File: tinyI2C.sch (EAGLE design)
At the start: 28 parts, among them IC1 74ABT125BQ, IC2 TPS76318, U1 LPC824M201JHI33, X1 TSW-112-02-S-S, X2 TSW-106-02-S-S-RA, X3 TSW-112-02-S-S, X4 TSW-102-02-S-S

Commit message: fiducials
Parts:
- added TP4, TP5: TPTP10R, testpad:TPTP10R
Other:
- note added: "FIDUCIALS"
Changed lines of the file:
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@@
 <part name="X4" library="con-samtec.local" deviceset="TSW-102-02-S-S" device=""/>
 <part name="GND12" library="mbed-HDK" deviceset="GND" device=""/>
+<part name="TP4" library="testpad" deviceset="TP" device="TP10R" value="TPTP10R"/>
+<part name="TP5" library="testpad" deviceset="TP" device="TP10R" value="TPTP10R"/>
 </parts>
 <sheets>
 <sheet>
 <plain>
+<text x="231.14" y="40.64" size="1.778" layer="91">FIDUCIALS</text>
 </plain>
 <instances>
@@
 <instance part="X4" gate="-2" x="83.82" y="122.428" rot="MR0"/>
 <instance part="GND12" gate="1" x="86.36" y="122.428"/>
+<instance part="TP4" gate="G$1" x="238.76" y="48.26" smashed="yes" rot="R90">
+<attribute name="NAME" x="238.252" y="47.244" size="1.778" layer="95" rot="MR0"/>
+<attribute name="TP_SIGNAL_NAME" x="240.03" y="49.53" size="1.778" layer="97" rot="R90"/>
+</instance>
+<instance part="TP5" gate="G$1" x="238.76" y="45.72" smashed="yes" rot="R90">
+<attribute name="NAME" x="238.252" y="44.704" size="1.778" layer="95" rot="MR0"/>
+<attribute name="TP_SIGNAL_NAME" x="240.03" y="46.99" size="1.778" layer="97" rot="R90"/>
+</instance>
 </instances>
 <busses>
@@
 </segment>
 </net>
+<net name="N$2" class="0">
+<segment>
+<wire x1="228.6" y1="53.34" x2="246.38" y2="53.34" width="0.1524" layer="91"/>
+<wire x1="246.38" y1="53.34" x2="246.38" y2="38.1" width="0.1524" layer="91"/>
+<wire x1="246.38" y1="38.1" x2="228.6" y2="38.1" width="0.1524" layer="91"/>
+<wire x1="228.6" y1="38.1" x2="228.6" y2="53.34" width="0.1524" layer="91"/>
+</segment>
+</net>

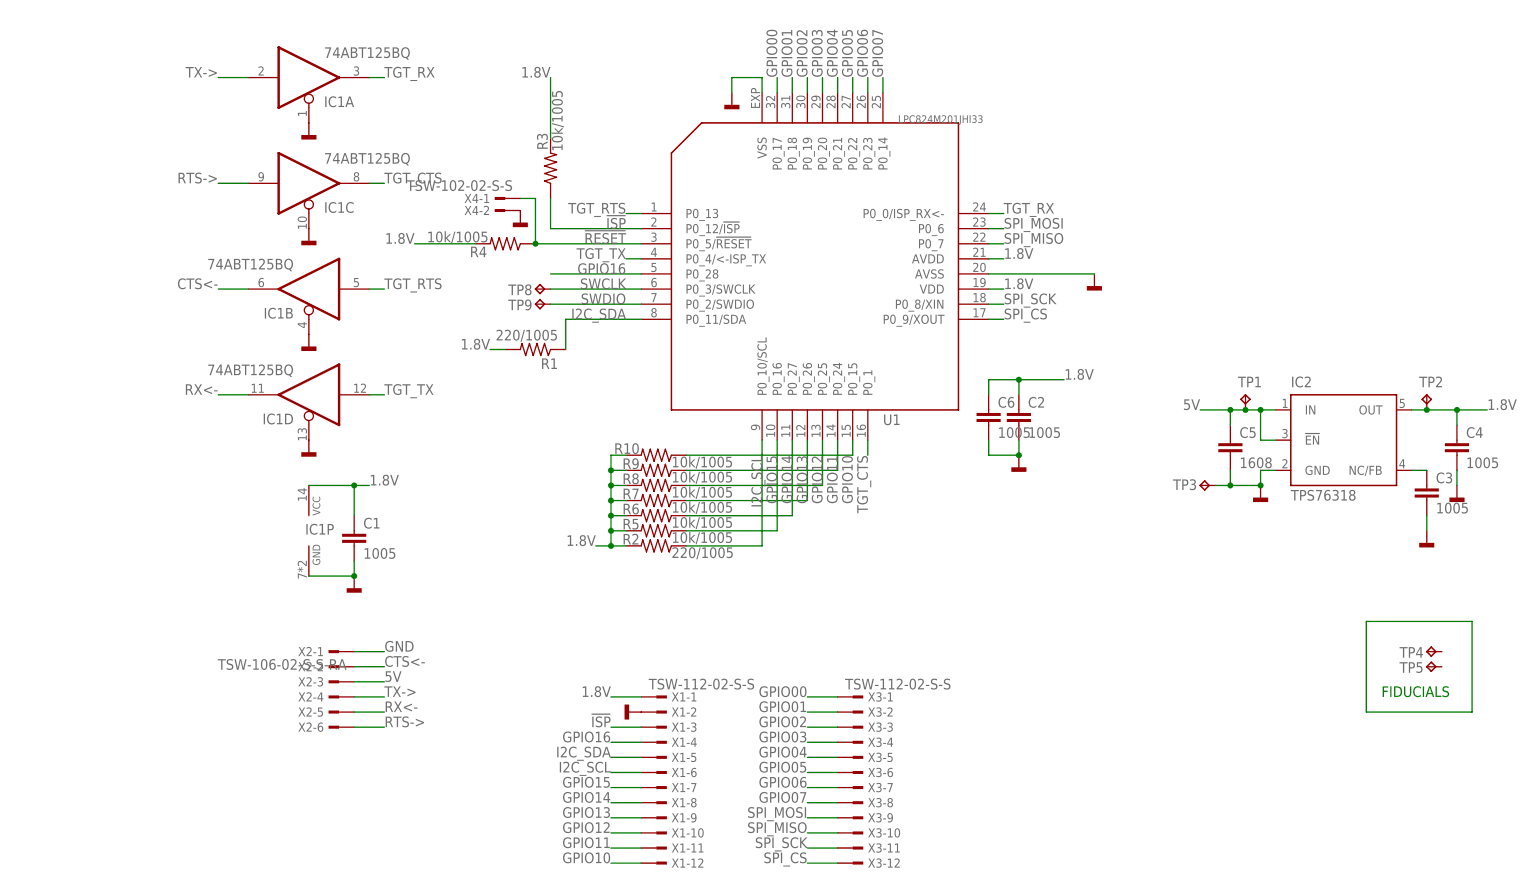
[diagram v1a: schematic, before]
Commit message: panelize update
each edge has 0.4mm margin
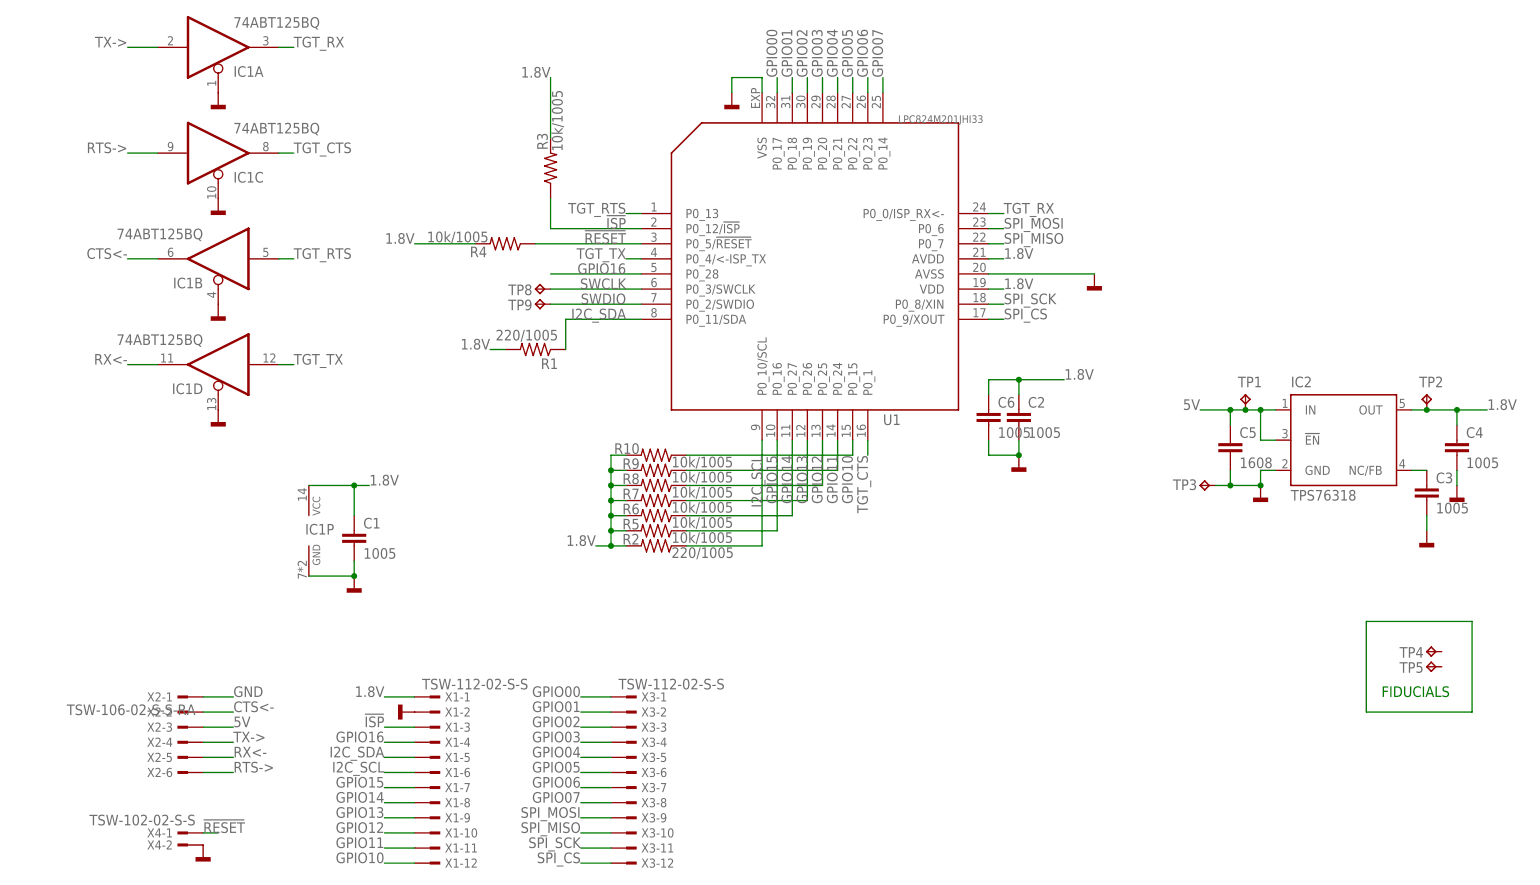
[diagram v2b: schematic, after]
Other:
- moved on the sheet: IC1A, IC1B, IC1C, IC1D, X1-1, X1-10, X1-11, X1-12, X1-2, X1-3, X1-4, X1-5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
